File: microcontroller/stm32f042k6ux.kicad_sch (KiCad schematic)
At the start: 20 parts, among them J3 TC2030, U5 STM32F042K6Ux, Y2 ECS-160-10-36Q-AES-TR

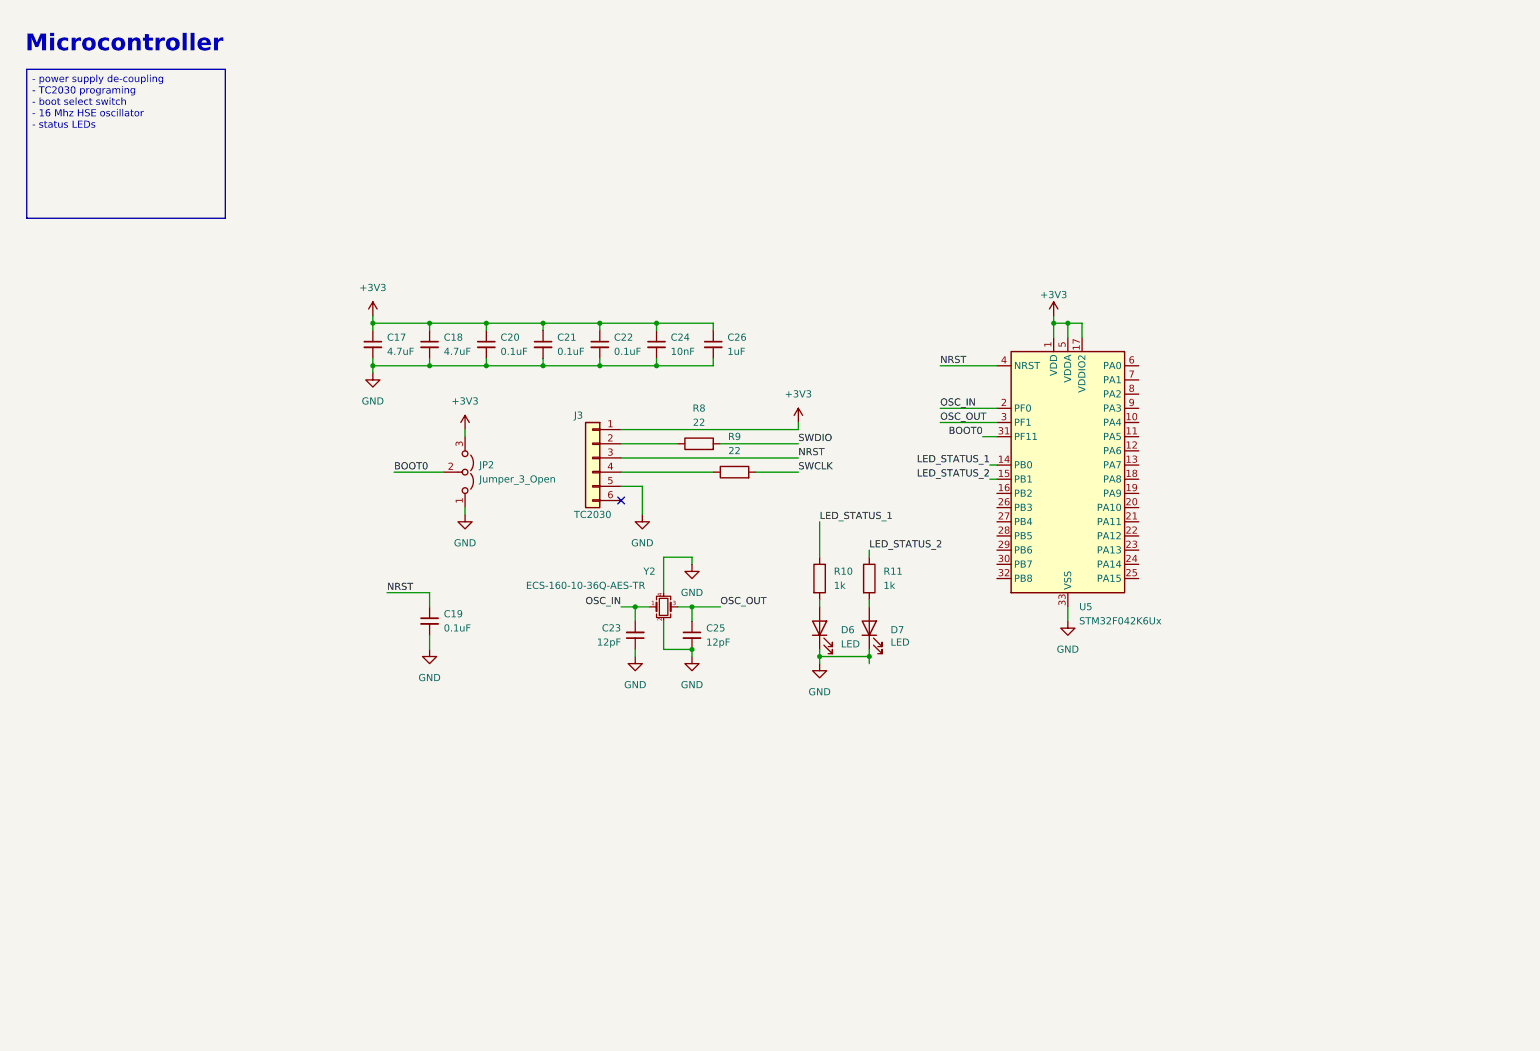
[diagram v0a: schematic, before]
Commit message: Added SWIO net labels to micro
Organized sheet, added NRST test point
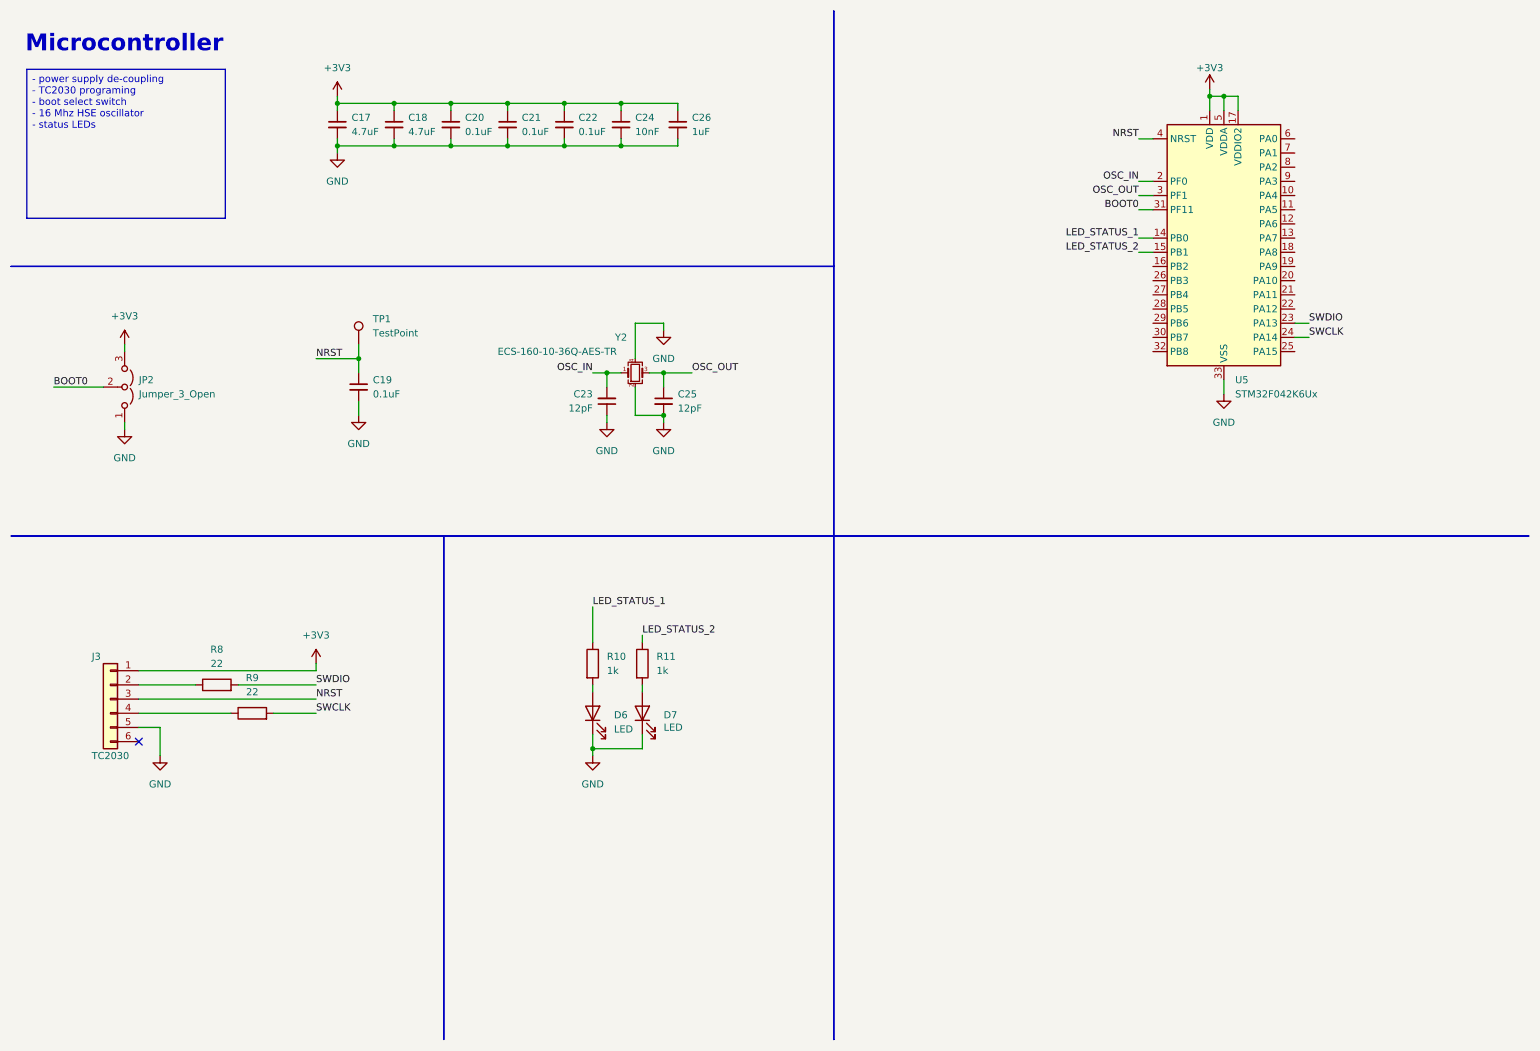
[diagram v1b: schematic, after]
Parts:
- added TP1: TestPoint, symbol Connector:TestPoint
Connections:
- net NRST: now also TP1.1
- net SWCLK: now also U5.24 (PA14)
- net SWDIO: now also U5.23 (PA13)
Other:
- moved on the sheet: C17, C18, C19, C20, C21, C22, C23, C24, C25, C26, D6, D7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

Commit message: Updated STM32 with different VCC symbol
- Added more integration details
- Added note regarding TCAN compatability to can tranciever schematic
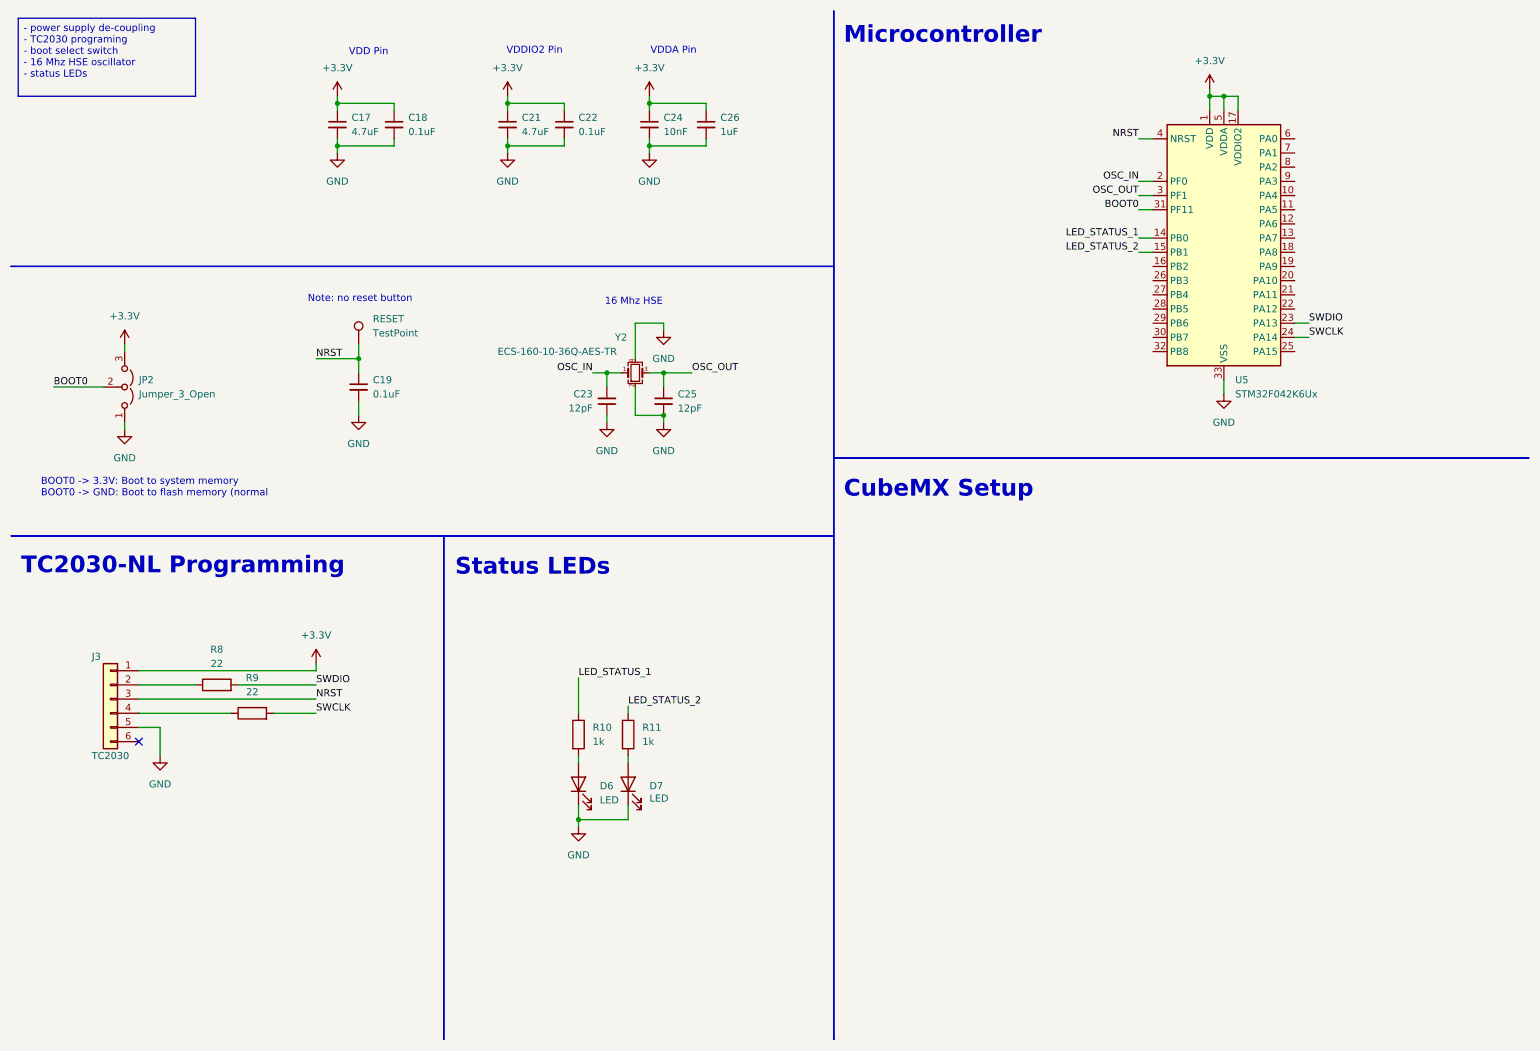
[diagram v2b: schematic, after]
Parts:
- removed C20: 0.1uF, Capacitor_SMD:C_0603_1608Metric, symbol Device:C_Small
- C18: value 4.7uF -> 0.1uF
- C21: value 0.1uF -> 4.7uF
- renumbered TP1 to RESET
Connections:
- net +3V3 renamed +3.3V
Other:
- note added: "16 Mhz HSE"
- note added: "BOOT0 -> 3.3V: Boot to system memory BOOT0 -> GND: Boot to flash memory (normal"
- note added: "CubeMX Setup"
- note added: "Note: no reset button"
- note added: "Status LEDs"
- note added: "TC2030-NL Programming"
- note added: "VDD Pin"
- note added: "VDDA Pin"
- note added: "VDDIO2 Pin"
- moved on the sheet: C24, C26, D6, D7, R10, R11
